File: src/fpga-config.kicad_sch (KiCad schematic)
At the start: 0 parts

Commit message: Adds symbol for DDR2
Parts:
- added C45, C49: 0.47u, symbol Device:C_Small
- added C46, C47, C48: 100n, symbol Device:C_Small
- added D1: RED, symbol Device:LED
- added D2: GREEN, symbol Device:LED
- added Q1: 2N2222, symbol Simulation_SPICE:NPN
- added R1, R12, R14: 4.7k, symbol Device:R_Small
- added R15, R16, R17, R19, R22, R23: 10k, symbol Device:R_Small
- added R18: 1k, symbol Device:R_Small
- added R20, R21: ?, symbol Device:R_Small
- added U2: ~, symbol ECAP5-BSOM:LFE5U-85F-*BG756*
- added U6: W25Q128JVPIM, symbol ECAP5-BSOM:W25Q128JVPIM
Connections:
- new net: D1.2 (A), R20.2, R21.1
- new net: D2.2 (A), R21.2
- new net: D2.1 (K), Q1.1 (C)
- new net: Q1.2 (B), R22.1
- new net +3V3: C45.1, C46.1, C47.1, C49.1, R1.1, R15.2, R16.2, R17.2, R18.2, R19.2, R20.1, R23.2, U2. (VCCIO8[2]), U2.AB10 (VCCIO8), U2.AC10 (VCCIO8), U6.8 (VCC)
- new net CFG.CLK: R18.1, U2.AM3 (CCLK/MCLK/SCK), U6.6 (CLK)
- new net CFG.CS: R23.1, U2.AJ3 (PB15A/HOLDN/DI/BUSY/CSSPIN/CEN), U6.1 (~{CS})
- new net CFG.DONE: R22.2, U2.AJ4 (DONE)
- new net CFG.INITN: D1.1 (K), U2.AG4 (INITN)
- new net CFG.IO0: R15.1, U2.AK2 (PB11B/D0/MOSI/IO0), U6.5 (DI/IO0)
- new net CFG.IO1: R16.1, U2.AJ2 (PB11A/D1/MISO/IO1), U6.2 (DO/IO1)
- new net CFG.IO2: R17.1, U2.AM2 (PB9B/D2/IO2), U6.3 (~{WP}/IO2)
- new net CFG.IO3: R19.1, U2.AL1 (PB9A/D3/IO3), U6.7 (~{HOLD}/IO3)
- new net CFG0: R14.2, U2.AM4 (CFG_0)
- new net CFG1: R1.2, U2.AL4 (CFG_1)
- new net CFG2: R12.2, U2.AK4 (CFG_2)
- new net GND: C45.2, C46.2, C47.2, C48.2, C49.2, Q1.3 (E), R12.1, R14.1, U6.4 (GND)
- new net IO.RESET: C48.1, U2.AH4 (PROGRAMN)

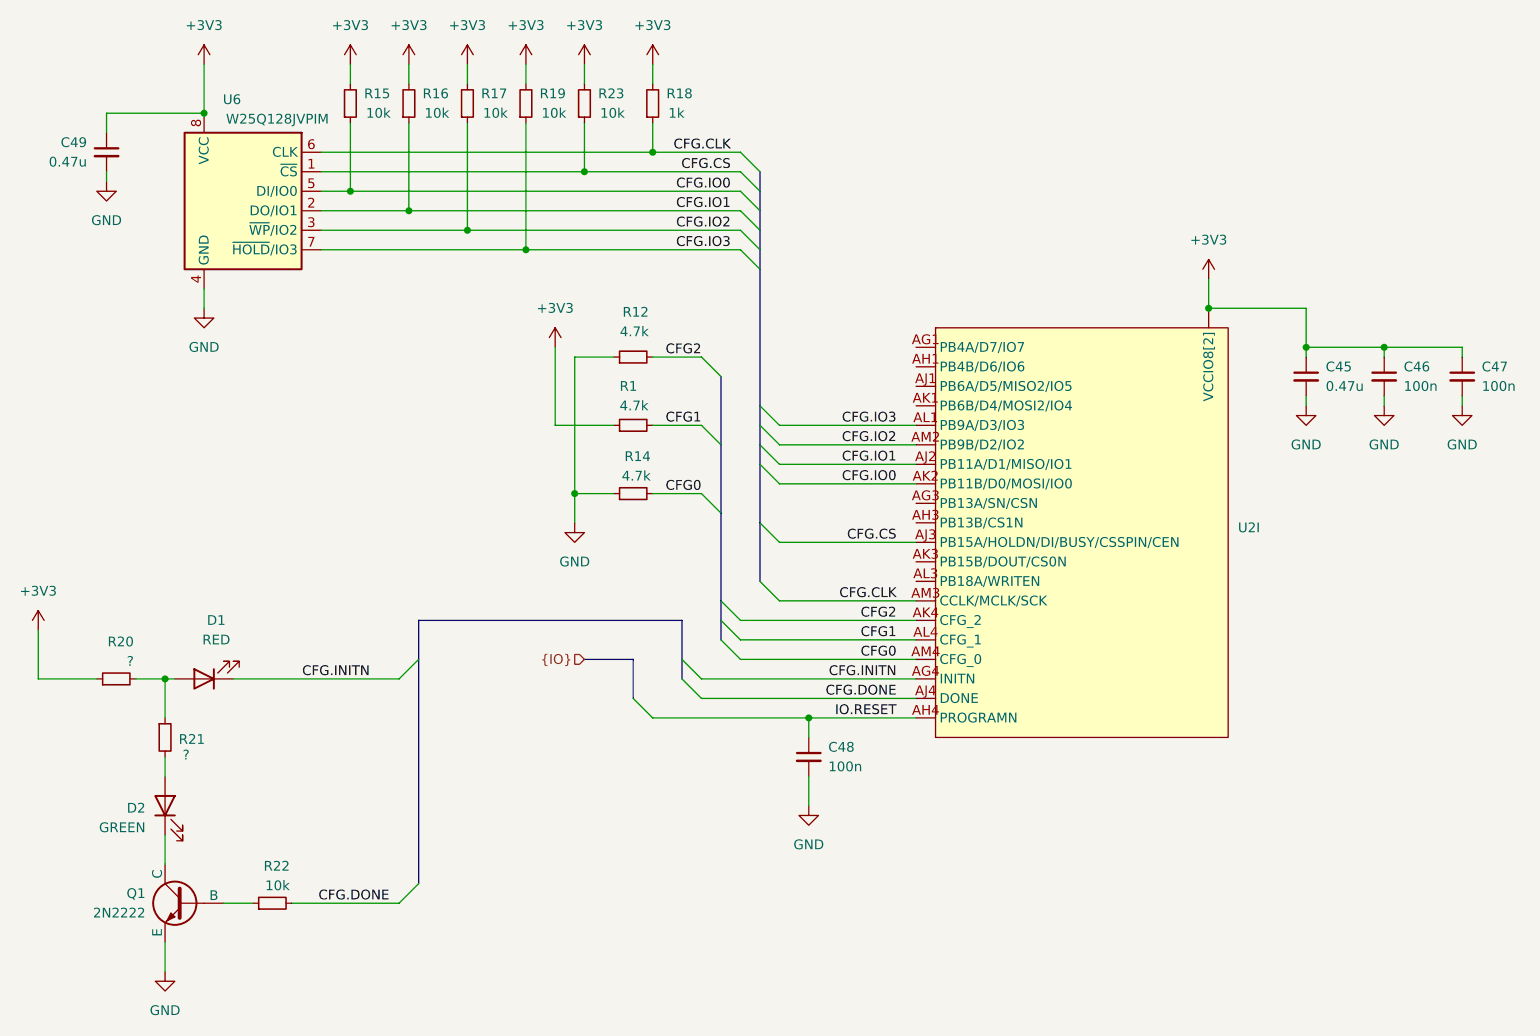
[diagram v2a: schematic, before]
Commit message: Adds DDR2 schematic
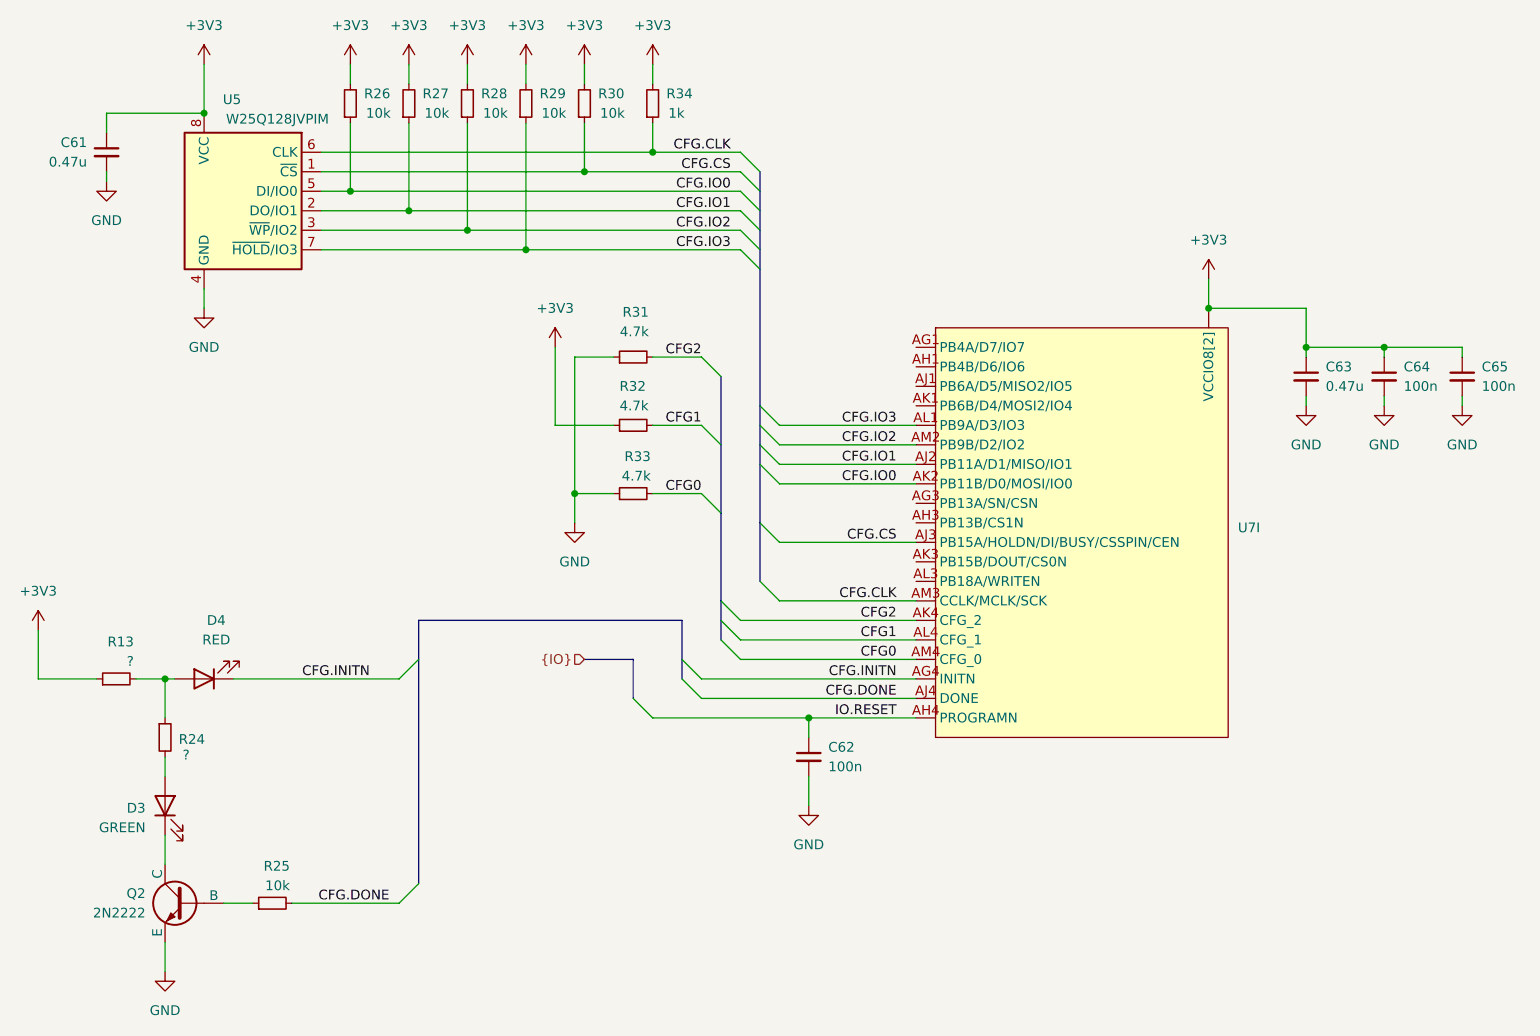
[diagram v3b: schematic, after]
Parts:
- renumbered C49 to C61, C48 to C62, C45 to C63, C46 to C64, C47 to C65, D2 to D3, D1 to D4, Q1 to Q2, R20 to R13, R21 to R24, R22 to R25, R15 to R26, R16 to R27, R17 to R28, R19 to R29, R23 to R30, R12 to R31, R1 to R32, R14 to R33, R18 to R34, U6 to U5, U2 to U7
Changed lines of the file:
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@@
 		(on_board yes)
 		(dnp no)
-		(property "Reference" "U6"
+		(property "Reference" "U5"
 			(at 79.756 42.672 0)
 			(effects
@@
 		(dnp no)
 		(fields_autoplaced yes)
-		(property "Reference" "U2"
+		(property "Reference" "U7"
 			(at 209.55 98.4249 0)
 			(effects
@@
 		(dnp no)
 		(fields_autoplaced yes)
-		(property "Reference" "#PWR09"
+		(property "Reference" "#PWR066"
 			(at 123.19 104.14 0)
 			(effects
@@
 		(on_board yes)
 		(dnp no)
-		(property "Reference" "R19"
+		(property "Reference" "R29"
 			(at 118.618 41.91 0)
 			(effects
@@
 		(dnp no)
 		(fields_autoplaced yes)
-		(property "Reference" "#PWR047"
+		(property "Reference" "#PWR064"
 			(at 116.84 41.91 0)
 			(effects
@@
 		(dnp no)
 		(fields_autoplaced yes)
-		(property "Reference" "#PWR048"
+		(property "Reference" "#PWR068"
 			(at 133.35 41.91 0)
 			(effects
@@
 		(dnp no)
 		(fields_autoplaced yes)
-		(property "Reference" "C47"
+		(property "Reference" "C65"
 			(at 241.3 77.4762 0)
 			(effects
@@
 		(on_board yes)
 		(dnp no)
-		(property "Reference" "R17"
+		(property "Reference" "R28"
 			(at 110.998 41.91 0)
 			(effects
@@
 		(dnp no)
 		(fields_autoplaced yes)
-		(property "Reference" "C49"
+		(property "Reference" "C61"
 			(at 59.69 48.2662 0)
 			(effects
@@
 		(dnp no)
 		(fields_autoplaced yes)
-		(property "Reference" "#PWR051"
+		(property "Reference" "#PWR049"
 			(at 53.34 115.57 0)
 			(effects
@@
 		(on_board yes)
 		(dnp no)
-		(property "Reference" "R21"
+		(property "Reference" "R24"
 			(at 71.628 125.984 0)
 			(effects
@@
 		(on_board yes)
 		(dnp no)
-		(property "Reference" "R23"
+		(property "Reference" "R30"
 			(at 126.238 41.91 0)
 			(effects
@@
 		(on_board yes)
 		(dnp no)
-		(property "Reference" "R12"
+		(property "Reference" "R31"
 			(at 132.842 70.358 90)
 			(effects
@@
 		(dnp no)
 		(fields_autoplaced yes)
-		(property "Reference" "#PWR046"
+		(property "Reference" "#PWR063"
 			(at 109.22 41.91 0)
 			(effects
@@
 		(dnp no)
 		(fields_autoplaced yes)
-		(property "Reference" "#PWR043"
+		(property "Reference" "#PWR060"
 			(at 74.93 76.2 0)
 			(effects
@@
 		(dnp no)
 		(fields_autoplaced yes)
-		(property "Reference" "#PWR057"
+		(property "Reference" "#PWR067"
 			(at 124.46 41.91 0)
 			(effects
@@
 		(dnp no)
 		(fields_autoplaced yes)
-		(property "Reference" "#PWR01"
+		(property "Reference" "#PWR065"
 			(at 120.65 78.74 0)
 			(effects
@@
 		(dnp no)
 		(fields_autoplaced yes)
-		(property "Reference" "#PWR012"
+		(property "Reference" "#PWR071"
 			(at 218.44 88.9 0)
 			(effects
@@
 		(dnp no)
 		(fields_autoplaced yes)
-		(property "Reference" "#PWR045"
+		(property "Reference" "#PWR062"
 			(at 101.6 41.91 0)
 			(effects
@@
 		(dnp no)
 		(fields_autoplaced yes)
-		(property "Reference" "#PWR044"
+		(property "Reference" "#PWR061"
 			(at 93.98 41.91 0)
 			(effects
@@
 		(dnp no)
 		(fields_autoplaced yes)
-		(property "Reference" "#PWR029"
+		(property "Reference" "#PWR073"
 			(at 238.76 88.9 0)
 			(effects
@@
 		(on_board yes)
 		(dnp no)
-		(property "Reference" "R1"
+		(property "Reference" "R32"
 			(at 129.032 80.01 90)
 			(effects
@@
 		(dnp no)
 		(fields_autoplaced yes)
-		(property "Reference" "#PWR041"
+		(property "Reference" "#PWR059"
 			(at 74.93 41.91 0)
 			(effects
@@
 		(dnp no)
 		(fields_autoplaced yes)
-		(property "Reference" "#PWR052"
+		(property "Reference" "#PWR058"
 			(at 69.85 162.56 0)
 			(effects
@@
 		(dnp no)
 		(fields_autoplaced yes)
-		(property "Reference" "#PWR050"
+		(property "Reference" "#PWR069"
 			(at 153.67 140.97 0)
 			(effects
@@
 		(on_board yes)
 		(dnp no)
-		(property "Reference" "R20"
+		(property "Reference" "R13"
 			(at 65.786 113.284 90)
 			(effects
@@
 		(dnp no)
 		(fields_autoplaced yes)
-		(property "Reference" "#PWR024"
+		(property "Reference" "#PWR072"
 			(at 228.6 88.9 0)
 			(effects
@@
 		(dnp no)
 		(fields_autoplaced yes)
-		(property "Reference" "#PWR040"
+		(property "Reference" "#PWR070"
 			(at 205.74 69.85 0)
 			(effects
@@
 		(dnp no)
 		(fields_autoplaced yes)
-		(property "Reference" "#PWR042"
+		(property "Reference" "#PWR056"
 			(at 62.23 59.69 0)
 			(effects
@@
 		(dnp no)
 		(fields_autoplaced yes)
-		(property "Reference" "C45"
+		(property "Reference" "C63"
 			(at 220.98 77.4762 0)
 			(effects
@@
 		(dnp no)
 		(fields_autoplaced yes)
-		(property "Reference" "Q1"
+		(property "Reference" "Q2"
 			(at 67.31 146.0499 0)
 			(effects
@@
 		(on_board yes)
 		(dnp no)
-		(property "Reference" "R16"
+		(property "Reference" "R27"
 			(at 103.378 41.91 0)
 			(effects
@@
 		(dnp no)
 		(fields_autoplaced yes)
-		(property "Reference" "D1"
+		(property "Reference" "D4"
 			(at 76.5175 110.49 0)
 			(effects
@@
 		(on_board yes)
 		(dnp no)
-		(property "Reference" "R15"
+		(property "Reference" "R26"
 			(at 95.758 41.91 0)
 			(effects
@@
 		(dnp no)
 		(fields_autoplaced yes)
-		(property "Reference" "C46"
+		(property "Reference" "C64"
 			(at 231.14 77.4762 0)
 			(effects
@@
 		(dnp no)
 		(fields_autoplaced yes)
-		(property "Reference" "D2"
+		(property "Reference" "D3"
 			(at 67.31 134.9374 90)
 			(effects
@@
 		(on_board yes)
 		(dnp no)
-		(property "Reference" "R14"
+		(property "Reference" "R33"
 			(at 133.096 89.154 90)
 			(effects
@@
 		(on_board yes)
 		(dnp no)
-		(property "Reference" "R22"
+		(property "Reference" "R25"
 			(at 86.106 142.494 90)
 			(effects
@@
 		(dnp no)
 		(fields_autoplaced yes)
-		(property "Reference" "C48"
+		(property "Reference" "C62"
 			(at 156.21 127.0062 0)
 			(effects
@@
 		(on_board yes)
 		(dnp no)
-		(property "Reference" "R18"
+		(property "Reference" "R34"
 			(at 135.128 41.91 0)
 			(effects

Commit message: Add the eMMC
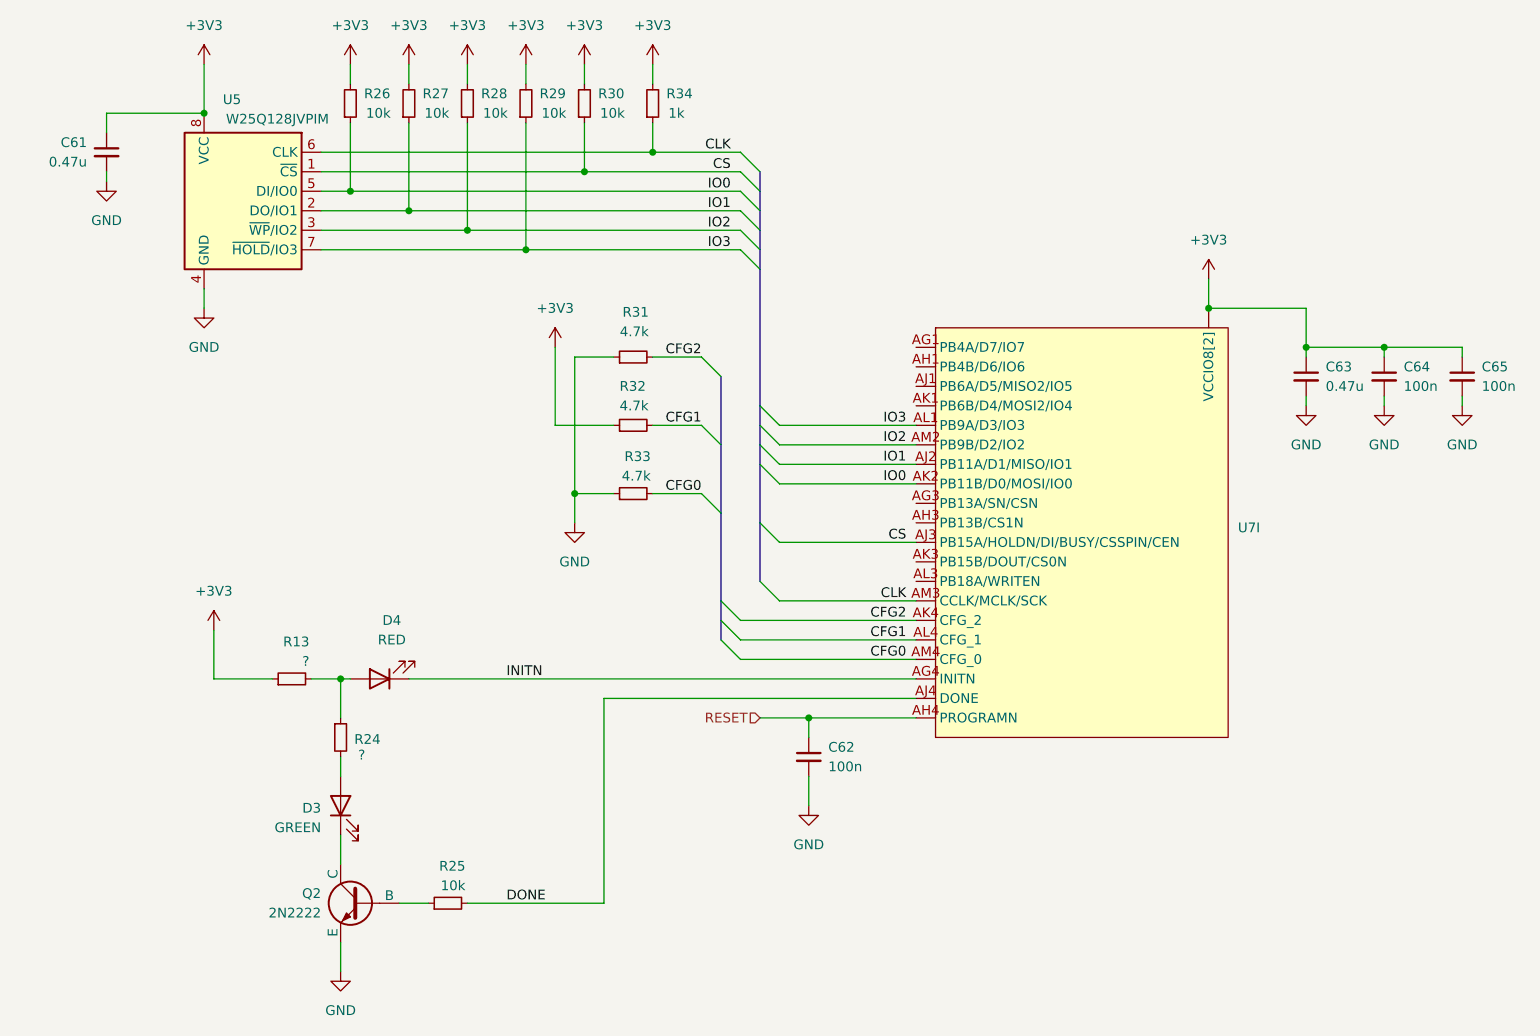
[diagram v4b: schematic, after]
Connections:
- net CFG.CLK renamed CLK
- net CFG.CS renamed CS
- net CFG.DONE renamed DONE
- net CFG.INITN renamed INITN
- net CFG.IO0 renamed IO0
- net CFG.IO1 renamed IO1
- net CFG.IO2 renamed IO2
- net CFG.IO3 renamed IO3
- net IO.RESET renamed RESET
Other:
- moved on the sheet: D3, D4, Q2, R13, R24, R25
